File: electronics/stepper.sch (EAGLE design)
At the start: 10 parts, among them U1 STEPPER-DRIVER-AP1034STEPPER-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

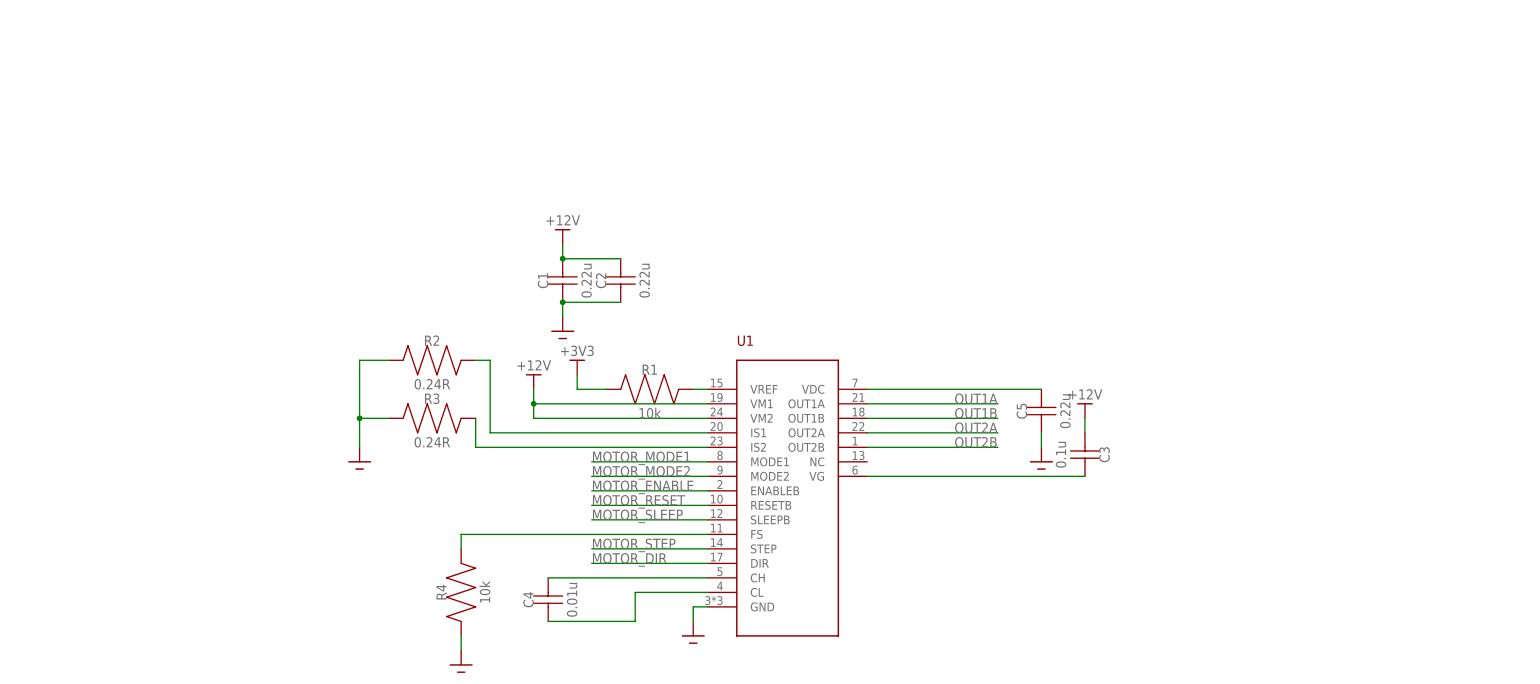
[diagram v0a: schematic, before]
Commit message: Everything on the stepper driver schematic except the JST connectors for the motors
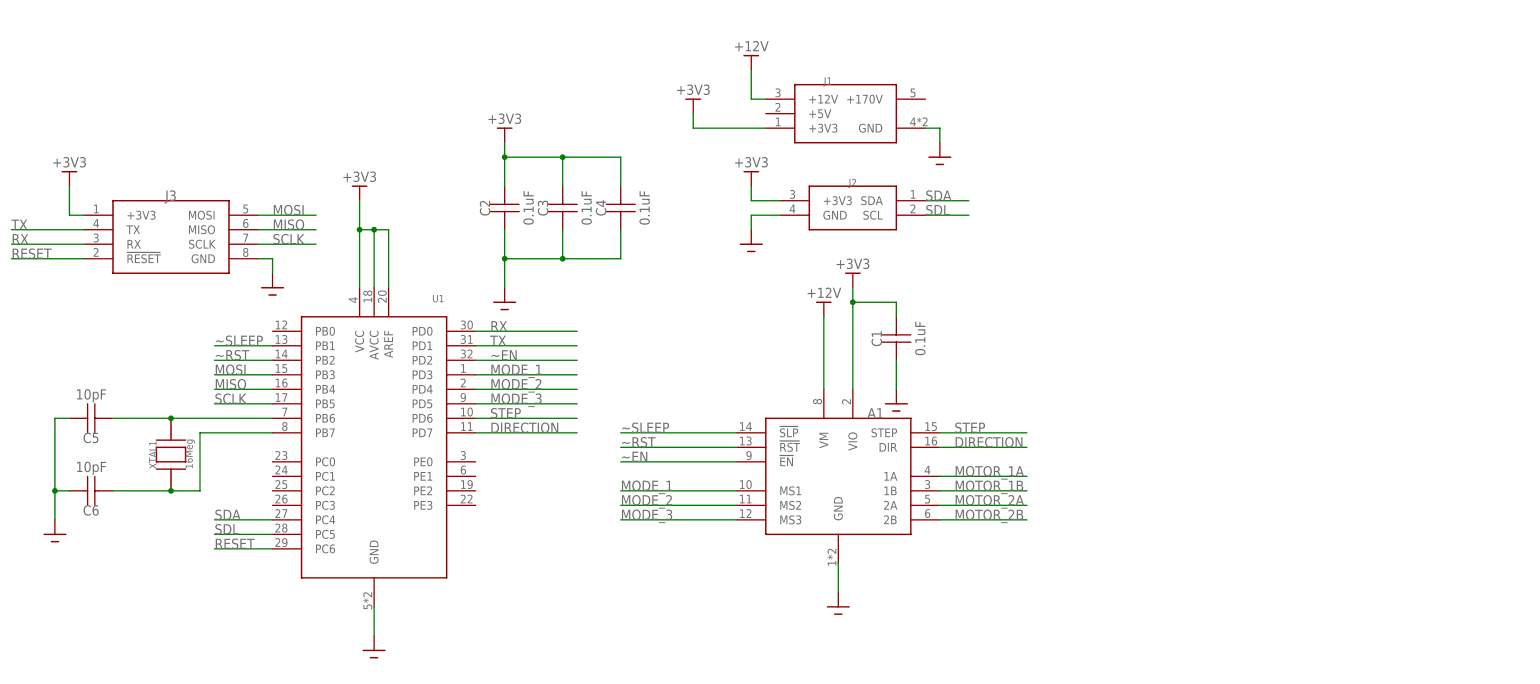
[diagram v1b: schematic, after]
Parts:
- removed R1, R4: 10k, Zach:RESISTOR0805
- removed R2, R3: 0.24R, Zach:RESISTOR0805
- added A1: STEPPER_DRIVER, Zach:STEPPER_DRIVER
- added C6: 10pF, Zach:CAPACITOR0402
- added J1: 1-770969-0, Zach:1-770969-0
- added J2: 1-770968-0, Zach:1-770968-0
- added J3: DF1BZ-8DP-2.5DSA, Zach:DF1BZ-8DP-2.5DSA
- added XTAL1: 16Meg, Zach:XRCGB
- C1, C2: value 0.22u -> 0.1uF; device Zach:CAPACITOR0805 -> Zach:CAPACITOR0402
- C3: value 0.1u -> 0.1uF; device Zach:CAPACITOR0805 -> Zach:CAPACITOR0402
- C4: value 0.01u -> 0.1uF; device Zach:CAPACITOR0805 -> Zach:CAPACITOR0402
- C5: value 0.22u -> 10pF; device Zach:CAPACITOR0805 -> Zach:CAPACITOR0402
- U1: value STEPPER-DRIVER-AP1034STEPPER-DRIVER-AP1034 -> ATMEGA328PB32-TQFP; device Miranda:STEPPER-DRIVER-AP1034STEPPER-DRIVER-AP1034 -> Zach:ATMEGA328PB32-TQFP
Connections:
- removed net MOTOR_DIR: U1.DIR
- removed net MOTOR_ENABLE: U1.ENABLEB
- removed net MOTOR_MODE1: U1.MODE1
- removed net MOTOR_MODE2: U1.MODE2
- removed net MOTOR_RESET: U1.RESETB
- removed net MOTOR_SLEEP: U1.SLEEPB
- removed net MOTOR_STEP: U1.STEP
- removed net N$3: R3.P$2, U1.IS2
- removed net N$4: R2.P$2, U1.IS1
- removed net N$5: C4.P$2, U1.CH
- removed net N$6: C4.P$1, U1.CL
- removed net N$7: R4.P$2, U1.FS
- removed net N$8: C5.P$2, U1.VDC
- removed net OUT1A: U1.OUT1A
- removed net OUT1B: U1.OUT1B
- removed net OUT2A: U1.OUT2A
- removed net OUT2B: U1.OUT2B
- new net DIRECTION: A1.DIR, U1.PD7
- new net MISO: J3.MISO, U1.PB4
- new net MODE_1: A1.MS1, U1.PD3
- new net MODE_2: A1.MS2, U1.PD4
- new net MODE_3: A1.MS3, U1.PD5
- new net MOSI: J3.MOSI, U1.PB3
- new net MOTOR_1A: A1.1A
- new net MOTOR_1B: A1.1B
- new net MOTOR_2A: A1.2A
- new net MOTOR_2B: A1.2B
- new net RESET: J3.!RESET, U1.PC6
- new net RX: J3.RX, U1.PD0
- new net SCLK: J3.SCLK, U1.PB5
- new net SDA: J2.SDA, U1.PC4
- new net SDL: J2.SCL, U1.PC5
- new net STEP: A1.STEP, U1.PD6
- new net TX: J3.TX, U1.PD1
- new net ~EN: A1.!EN, U1.PD2
- new net ~RST: A1.!RST, U1.PB2
- new net ~SLEEP: A1.!SLP, U1.PB1
- net +12V: now also A1.VM, J1.+12V; no longer C1.P$2, C2.P$2, C3.P$1, U1.VM1, U1.VM2
- net +3V3: now also A1.VIO, C1.P$2, C2.P$2, C3.P$2, C4.P$2, J1.+3V3, J2.+3V3, J3.+3V3, U1.AREF, U1.AVCC, U1.VCC; no longer R1.P$1
- net GND: now also A1.GND, C3.P$1, C4.P$1, C5.P$2, C6.P$2, J1.GND, J2.GND, J3.GND; no longer C5.P$1, R2.P$1, R3.P$1, R4.P$1
- net N$1: now also C5.P$1, U1.PB6, XTAL1.P$2; no longer C3.P$2, U1.VG
- net N$2: now also C6.P$1, U1.PB7, XTAL1.P$1; no longer R1.P$2, U1.VREF
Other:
- moved on the sheet: C1, C2, C3, C4, C5

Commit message: Stepper schematic is done. Ready for checkover
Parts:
- added J4: S4B-XH-A, Zach:S4B-XH-A
- added R1, R2, R3, R4: 0R, Zach:RESISTOR0402
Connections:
- new net N$3: J4.2, R3.P$1, R4.P$1
- new net N$5: J4.3, R1.P$1, R2.P$1
- net MOTOR_1A: now also J4.1
- net MOTOR_1B: now also R2.P$2, R4.P$2
- net MOTOR_2A: now also R1.P$2, R3.P$2
- net MOTOR_2B: now also J4.4
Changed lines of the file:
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@@
 <part name="P+8" library="Zach" deviceset="+3V3" device=""/>
 <part name="GND8" library="Zach" deviceset="GND" device=""/>
+<part name="J4" library="Zach" deviceset="S4B-XH-A" device="" package3d_urn="urn:adsk.eagle:package:16760823/1"/>
+<part name="R1" library="Zach" deviceset="RESISTOR" device="0402" value="0R"/>
+<part name="R2" library="Zach" deviceset="RESISTOR" device="0402" value="0R"/>
+<part name="R3" library="Zach" deviceset="RESISTOR" device="0402" value="0R"/>
+<part name="R4" library="Zach" deviceset="RESISTOR" device="0402" value="0R"/>
 </parts>
 <sheets>
@@
 </instance>
 <instance part="GND8" gate="1" x="-66.04" y="45.72" smashed="yes"/>
+<instance part="J4" gate="G$1" x="152.4" y="53.34" smashed="yes">
+<attribute name="NAME" x="146.05" y="61.595" size="1.778" layer="95"/>
+</instance>
+<instance part="R1" gate="G$1" x="81.28" y="53.34" smashed="yes" rot="R90">
+<attribute name="NAME" x="78.74" y="60.96" size="1.778" layer="95" rot="R90" align="bottom-center"/>
+<attribute name="VALUE" x="86.36" y="60.96" size="1.778" layer="96" rot="R90" align="bottom-center"/>
+</instance>
+<instance part="R2" gate="G$1" x="93.98" y="53.34" smashed="yes" rot="R90">
+<attribute name="NAME" x="91.44" y="60.96" size="1.778" layer="95" rot="R90" align="bottom-center"/>
+<attribute name="VALUE" x="99.06" y="60.96" size="1.778" layer="96" rot="R90" align="bottom-center"/>
+</instance>
+<instance part="R3" gate="G$1" x="104.14" y="55.88" smashed="yes" rot="R90">
+<attribute name="NAME" x="101.6" y="63.5" size="1.778" layer="95" rot="R90" align="bottom-center"/>
+<attribute name="VALUE" x="109.22" y="63.5" size="1.778" layer="96" rot="R90" align="bottom-center"/>
+</instance>
+<instance part="R4" gate="G$1" x="116.84" y="55.88" smashed="yes" rot="R90">
+<attribute name="NAME" x="114.3" y="63.5" size="1.778" layer="95" rot="R90" align="bottom-center"/>
+<attribute name="VALUE" x="121.92" y="63.5" size="1.778" layer="96" rot="R90" align="bottom-center"/>
+</instance>
 </instances>
 <busses>
@@
 <label x="53.34" y="12.7" size="1.778" layer="95"/>
 </segment>
+<segment>
+<pinref part="J4" gate="G$1" pin="1"/>
+<wire x1="149.86" y1="58.42" x2="129.54" y2="58.42" width="0.1524" layer="91"/>
+<label x="129.54" y="58.42" size="1.778" layer="95"/>
+</segment>
 </net>
 <net name="MOTOR_1B" class="0">
@@
 <label x="53.34" y="10.16" size="1.778" layer="95"/>
 </segment>
+<segment>
+<pinref part="R2" gate="G$1" pin="P$2"/>
+<wire x1="93.98" y1="68.58" x2="93.98" y2="81.28" width="0.1524" layer="91"/>
+<wire x1="93.98" y1="81.28" x2="83.82" y2="81.28" width="0.1524" layer="91"/>
+<label x="83.82" y="81.28" size="1.778" layer="95"/>
+</segment>
+<segment>
+<pinref part="R4" gate="G$1" pin="P$2"/>
+<wire x1="116.84" y1="71.12" x2="116.84" y2="91.44" width="0.1524" layer="91"/>
+<wire x1="116.84" y1="91.44" x2="106.68" y2="91.44" width="0.1524" layer="91"/>
+<label x="106.68" y="91.44" size="1.778" layer="95"/>
+</segment>
 </net>
 <net name="MOTOR_2A" class="0">
@@
 <label x="53.34" y="7.62" size="1.778" layer="95"/>
 </segment>
+<segment>
+<pinref part="R1" gate="G$1" pin="P$2"/>
+<wire x1="81.28" y1="68.58" x2="81.28" y2="76.2" width="0.1524" layer="91"/>
+<wire x1="81.28" y1="76.2" x2="71.12" y2="76.2" width="0.1524" layer="91"/>
+<label x="71.12" y="76.2" size="1.778" layer="95"/>
+</segment>
+<segment>
+<pinref part="R3" gate="G$1" pin="P$2"/>
+<wire x1="104.14" y1="71.12" x2="104.14" y2="86.36" width="0.1524" layer="91"/>
+<wire x1="104.14" y1="86.36" x2="96.52" y2="86.36" width="0.1524" layer="91"/>
+<label x="96.52" y="86.36" size="1.778" layer="95"/>
+</segment>
 </net>
 <net name="MOTOR_2B" class="0">
@@
 <wire x1="50.8" y1="5.08" x2="66.04" y2="5.08" width="0.1524" layer="91"/>
 <label x="53.34" y="5.08" size="1.778" layer="95"/>
+</segment>
+<segment>
+<pinref part="J4" gate="G$1" pin="4"/>
+<wire x1="149.86" y1="50.8" x2="129.54" y2="50.8" width="0.1524" layer="91"/>
+<label x="129.54" y="50.8" size="1.778" layer="95"/>
 </segment>
 </net>
@@
 </segment>
 </net>
+<net name="N$3" class="0">
+<segment>
+<pinref part="R3" gate="G$1" pin="P$1"/>
+<pinref part="J4" gate="G$1" pin="2"/>
+<wire x1="104.14" y1="55.88" x2="116.84" y2="55.88" width="0.1524" layer="91"/>
+<pinref part="R4" gate="G$1" pin="P$1"/>
+<wire x1="116.84" y1="55.88" x2="149.86" y2="55.88" width="0.1524" layer="91"/>
+<junction x="116.84" y="55.88"/>
+</segment>
+</net>
+<net name="N$5" class="0">
+<segment>
+<pinref part="J4" gate="G$1" pin="3"/>
+<pinref part="R1" gate="G$1" pin="P$1"/>
+<wire x1="149.86" y1="53.34" x2="93.98" y2="53.34" width="0.1524" layer="91"/>
+<pinref part="R2" gate="G$1" pin="P$1"/>
+<wire x1="93.98" y1="53.34" x2="81.28" y2="53.34" width="0.1524" layer="91"/>
+<junction x="93.98" y="53.34"/>
+</segment>
+</net>

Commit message: Routing crap
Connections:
- net ~RST renamed RST
- net ~SLEEP renamed SLEEP
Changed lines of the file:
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@@
 </segment>
 </net>
-<net name="~SLEEP" class="0">
+<net name="SLEEP" class="0">
 <segment>
 <pinref part="A1" gate="G$1" pin="!SLP"/>
@@
 </segment>
 </net>
-<net name="~RST" class="0">
+<net name="RST" class="0">
 <segment>
 <pinref part="A1" gate="G$1" pin="!RST"/>

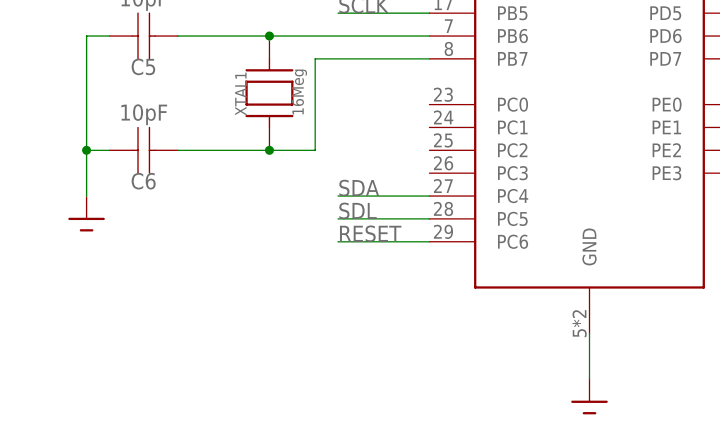
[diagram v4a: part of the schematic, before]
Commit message: Added pull-up on RESET
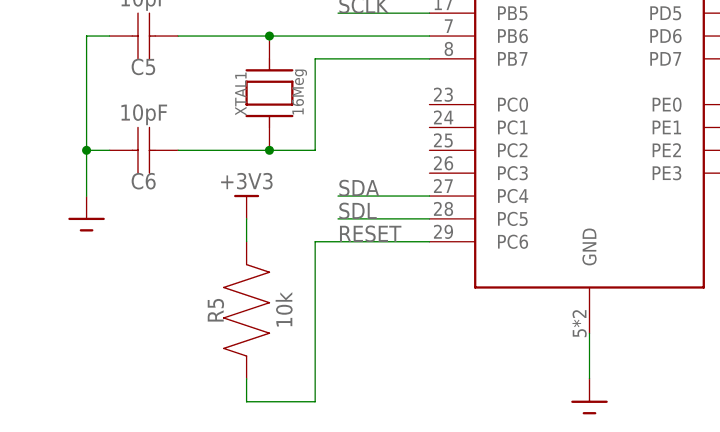
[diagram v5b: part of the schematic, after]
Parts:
- added R5: 10k, Zach:RESISTOR0805
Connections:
- net +3V3: now also R5.P$2
- net RESET: now also R5.P$1
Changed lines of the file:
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@@
 <part name="R3" library="Zach" deviceset="RESISTOR" device="0402" value="0R"/>
 <part name="R4" library="Zach" deviceset="RESISTOR" device="0402" value="0R"/>
+<part name="R5" library="Zach" deviceset="RESISTOR" device="0805" value="10k"/>
+<part name="P+9" library="Zach" deviceset="+3V3" device=""/>
 </parts>
 <sheets>
@@
 <attribute name="NAME" x="114.3" y="63.5" size="1.778" layer="95" rot="R90" align="bottom-center"/>
 <attribute name="VALUE" x="121.92" y="63.5" size="1.778" layer="96" rot="R90" align="bottom-center"/>
+</instance>
+<instance part="R5" gate="G$1" x="-86.36" y="-15.24" smashed="yes" rot="R90">
+<attribute name="NAME" x="-88.9" y="-7.62" size="1.778" layer="95" rot="R90" align="bottom-center"/>
+<attribute name="VALUE" x="-81.28" y="-7.62" size="1.778" layer="96" rot="R90" align="bottom-center"/>
+</instance>
+<instance part="P+9" gate="G$1" x="-86.36" y="5.08" smashed="yes">
+<attribute name="VALUE" x="-86.36" y="7.62" size="1.778" layer="96" rot="R180" align="bottom-center"/>
 </instance>
 </instances>
@@
 <wire x1="-101.6" y1="58.42" x2="-99.06" y2="58.42" width="0.1524" layer="91"/>
 </segment>
+<segment>
+<pinref part="R5" gate="G$1" pin="P$2"/>
+<pinref part="P+9" gate="G$1" pin="+3V3"/>
+<wire x1="-86.36" y1="0" x2="-86.36" y2="2.54" width="0.1524" layer="91"/>
+</segment>
 </net>
 <net name="SDL" class="0">
@@
 <segment>
 <pinref part="U1" gate="G$1" pin="PC6"/>
-<wire x1="-66.04" y1="0" x2="-76.2" y2="0" width="0.1524" layer="91"/>
+<wire x1="-66.04" y1="0" x2="-78.74" y2="0" width="0.1524" layer="91"/>
 <label x="-76.2" y="0" size="1.778" layer="95"/>
-</segment>
-</net>
+<pinref part="R5" gate="G$1" pin="P$1"/>
+<wire x1="-86.36" y1="-15.24" x2="-86.36" y2="-17.78" width="0.1524" layer="91"/>
+<wire x1="-86.36" y1="-17.78" x2="-78.74" y2="-17.78" width="0.1524" layer="91"/>
+<wire x1="-78.74" y1="-17.78" x2="-78.74" y2="0" width="0.1524" layer="91"/>
+</segment>
+</net>

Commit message: finished stepper
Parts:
- R5: device Zach:RESISTOR0805 -> Zach:RESISTOR0402
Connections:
- net DIRECTION: now also U1.PD2; no longer U1.PD7
- net MODE_1: now also U1.PD6; no longer U1.PD3
- net MODE_2: now also U1.PD5; no longer U1.PD4
- net MODE_3: now also U1.PE1; no longer U1.PD5
- net MOTOR_1A: now also A1.1B; no longer A1.1A
- net MOTOR_1B: now also A1.1A; no longer A1.1B
- net RST: now also U1.PE0; no longer U1.PB2
- net SLEEP: now also U1.PD4; no longer U1.PB1
- net STEP: now also U1.PD3; no longer U1.PD6
- net ~EN: now also U1.PD7; no longer U1.PD2
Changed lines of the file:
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@@
 <part name="R3" library="Zach" deviceset="RESISTOR" device="0402" value="0R"/>
 <part name="R4" library="Zach" deviceset="RESISTOR" device="0402" value="0R"/>
-<part name="R5" library="Zach" deviceset="RESISTOR" device="0805" value="10k"/>
+<part name="R5" library="Zach" deviceset="RESISTOR" device="0402" value="10k"/>
 <part name="P+9" library="Zach" deviceset="+3V3" device=""/>
 </parts>
@@
 </segment>
 <segment>
-<pinref part="U1" gate="G$1" pin="PB1"/>
-<wire x1="-66.04" y1="35.56" x2="-76.2" y2="35.56" width="0.1524" layer="91"/>
-<label x="-76.2" y="35.56" size="1.778" layer="95"/>
+<pinref part="U1" gate="G$1" pin="PD4"/>
+<wire x1="-30.48" y1="27.94" x2="-12.7" y2="27.94" width="0.1524" layer="91"/>
+<label x="-27.94" y="27.94" size="1.778" layer="95"/>
 </segment>
 </net>
@@
 </segment>
 <segment>
-<pinref part="U1" gate="G$1" pin="PB2"/>
-<wire x1="-66.04" y1="33.02" x2="-76.2" y2="33.02" width="0.1524" layer="91"/>
-<label x="-76.2" y="33.02" size="1.778" layer="95"/>
+<pinref part="U1" gate="G$1" pin="PE0"/>
+<wire x1="-30.48" y1="15.24" x2="-12.7" y2="15.24" width="0.1524" layer="91"/>
+<label x="-27.94" y="15.24" size="1.778" layer="95"/>
 </segment>
 </net>
@@
 </segment>
 <segment>
+<pinref part="U1" gate="G$1" pin="PD7"/>
+<wire x1="-30.48" y1="20.32" x2="-12.7" y2="20.32" width="0.1524" layer="91"/>
+<label x="-27.94" y="20.32" size="1.778" layer="95"/>
+</segment>
+</net>
+<net name="MODE_1" class="0">
+<segment>
+<pinref part="A1" gate="G$1" pin="MS1"/>
+<wire x1="15.24" y1="10.16" x2="-5.08" y2="10.16" width="0.1524" layer="91"/>
+<label x="-5.08" y="10.16" size="1.778" layer="95"/>
+</segment>
+<segment>
+<pinref part="U1" gate="G$1" pin="PD6"/>
+<wire x1="-30.48" y1="22.86" x2="-12.7" y2="22.86" width="0.1524" layer="91"/>
+<label x="-27.94" y="22.86" size="1.778" layer="95"/>
+</segment>
+</net>
+<net name="MODE_2" class="0">
+<segment>
+<pinref part="A1" gate="G$1" pin="MS2"/>
+<wire x1="15.24" y1="7.62" x2="-5.08" y2="7.62" width="0.1524" layer="91"/>
+<label x="-5.08" y="7.62" size="1.778" layer="95"/>
+</segment>
+<segment>
+<pinref part="U1" gate="G$1" pin="PD5"/>
+<wire x1="-30.48" y1="25.4" x2="-12.7" y2="25.4" width="0.1524" layer="91"/>
+<label x="-27.94" y="25.4" size="1.778" layer="95"/>
+</segment>
+</net>
+<net name="MODE_3" class="0">
+<segment>
+<pinref part="A1" gate="G$1" pin="MS3"/>
+<wire x1="15.24" y1="5.08" x2="-5.08" y2="5.08" width="0.1524" layer="91"/>
+<label x="-5.08" y="5.08" size="1.778" layer="95"/>
+</segment>
+<segment>
+<pinref part="U1" gate="G$1" pin="PE1"/>
+<wire x1="-30.48" y1="12.7" x2="-12.7" y2="12.7" width="0.1524" layer="91"/>
+<label x="-27.94" y="12.7" size="1.778" layer="95"/>
+</segment>
+</net>
+<net name="STEP" class="0">
+<segment>
+<pinref part="A1" gate="G$1" pin="STEP"/>
+<wire x1="50.8" y1="20.32" x2="66.04" y2="20.32" width="0.1524" layer="91"/>
+<label x="53.34" y="20.32" size="1.778" layer="95"/>
+</segment>
+<segment>
+<pinref part="U1" gate="G$1" pin="PD3"/>
+<wire x1="-30.48" y1="30.48" x2="-12.7" y2="30.48" width="0.1524" layer="91"/>
+<label x="-27.94" y="30.48" size="1.778" layer="95"/>
+</segment>
+</net>
+<net name="DIRECTION" class="0">
+<segment>
+<pinref part="A1" gate="G$1" pin="DIR"/>
+<wire x1="50.8" y1="17.78" x2="66.04" y2="17.78" width="0.1524" layer="91"/>
+<label x="53.34" y="17.78" size="1.778" layer="95"/>
+</segment>
+<segment>
 <pinref part="U1" gate="G$1" pin="PD2"/>
 <wire x1="-30.48" y1="33.02" x2="-12.7" y2="33.02" width="0.1524" layer="91"/>
@@
 </segment>
 </net>
-<net name="MODE_1" class="0">
-<segment>
-<pinref part="A1" gate="G$1" pin="MS1"/>
-<wire x1="15.24" y1="10.16" x2="-5.08" y2="10.16" width="0.1524" layer="91"/>
-<label x="-5.08" y="10.16" size="1.778" layer="95"/>
-</segment>
-<segment>
-<pinref part="U1" gate="G$1" pin="PD3"/>
-<wire x1="-30.48" y1="30.48" x2="-12.7" y2="30.48" width="0.1524" layer="91"/>
-<label x="-27.94" y="30.48" size="1.778" layer="95"/>
-</segment>
-</net>
-<net name="MODE_2" class="0">
-<segment>
-<pinref part="A1" gate="G$1" pin="MS2"/>
-<wire x1="15.24" y1="7.62" x2="-5.08" y2="7.62" width="0.1524" layer="91"/>
-<label x="-5.08" y="7.62" size="1.778" layer="95"/>
-</segment>
-<segment>
-<pinref part="U1" gate="G$1" pin="PD4"/>
-<wire x1="-30.48" y1="27.94" x2="-12.7" y2="27.94" width="0.1524" layer="91"/>
-<label x="-27.94" y="27.94" size="1.778" layer="95"/>
-</segment>
-</net>
-<net name="MODE_3" class="0">
-<segment>
-<pinref part="A1" gate="G$1" pin="MS3"/>
-<wire x1="15.24" y1="5.08" x2="-5.08" y2="5.08" width="0.1524" layer="91"/>
-<label x="-5.08" y="5.08" size="1.778" layer="95"/>
-</segment>
-<segment>
-<pinref part="U1" gate="G$1" pin="PD5"/>
-<wire x1="-30.48" y1="25.4" x2="-12.7" y2="25.4" width="0.1524" layer="91"/>
-<label x="-27.94" y="25.4" size="1.778" layer="95"/>
-</segment>
-</net>
-<net name="STEP" class="0">
-<segment>
-<pinref part="A1" gate="G$1" pin="STEP"/>
-<wire x1="50.8" y1="20.32" x2="66.04" y2="20.32" width="0.1524" layer="91"/>
-<label x="53.34" y="20.32" size="1.778" layer="95"/>
-</segment>
-<segment>
-<pinref part="U1" gate="G$1" pin="PD6"/>
-<wire x1="-30.48" y1="22.86" x2="-12.7" y2="22.86" width="0.1524" layer="91"/>
-<label x="-27.94" y="22.86" size="1.778" layer="95"/>
-</segment>
-</net>
-<net name="DIRECTION" class="0">
-<segment>
-<pinref part="A1" gate="G$1" pin="DIR"/>
-<wire x1="50.8" y1="17.78" x2="66.04" y2="17.78" width="0.1524" layer="91"/>
-<label x="53.34" y="17.78" size="1.778" layer="95"/>
-</segment>
-<segment>
-<pinref part="U1" gate="G$1" pin="PD7"/>
-<wire x1="-30.48" y1="20.32" x2="-12.7" y2="20.32" width="0.1524" layer="91"/>
-<label x="-27.94" y="20.32" size="1.778" layer="95"/>
-</segment>
-</net>
 <net name="MOTOR_1A" class="0">
-<segment>
-<pinref part="A1" gate="G$1" pin="1A"/>
-<wire x1="50.8" y1="12.7" x2="66.04" y2="12.7" width="0.1524" layer="91"/>
-<label x="53.34" y="12.7" size="1.778" layer="95"/>
-</segment>
 <segment>
 <pinref part="J4" gate="G$1" pin="1"/>
@@
 <label x="129.54" y="58.42" size="1.778" layer="95"/>
 </segment>
-</net>
-<net name="MOTOR_1B" class="0">
 <segment>
 <pinref part="A1" gate="G$1" pin="1B"/>
@@
 <label x="53.34" y="10.16" size="1.778" layer="95"/>
 </segment>
+</net>
+<net name="MOTOR_1B" class="0">
 <segment>
 <pinref part="R2" gate="G$1" pin="P$2"/>
@@
 <label x="106.68" y="91.44" size="1.778" layer="95"/>
 </segment>
-</net>
+<segment>
+<pinref part="A1" gate="G$1" pin="1A"/>
+<wire x1="50.8" y1="12.7" x2="66.04" y2="12.7" width="0.1524" layer="91"/>
+<label x="53.34" y="12.7" size="1.778" layer="95"/>
+</segment>
+</net>
